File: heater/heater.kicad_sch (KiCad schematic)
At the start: 2 parts, among them J1 Conn_01x01, J2 Conn_01x01

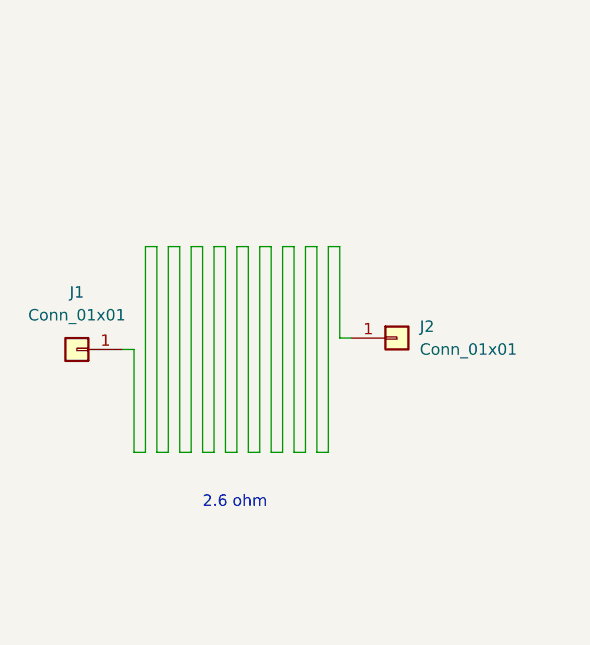
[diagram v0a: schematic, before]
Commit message: Design heating plate
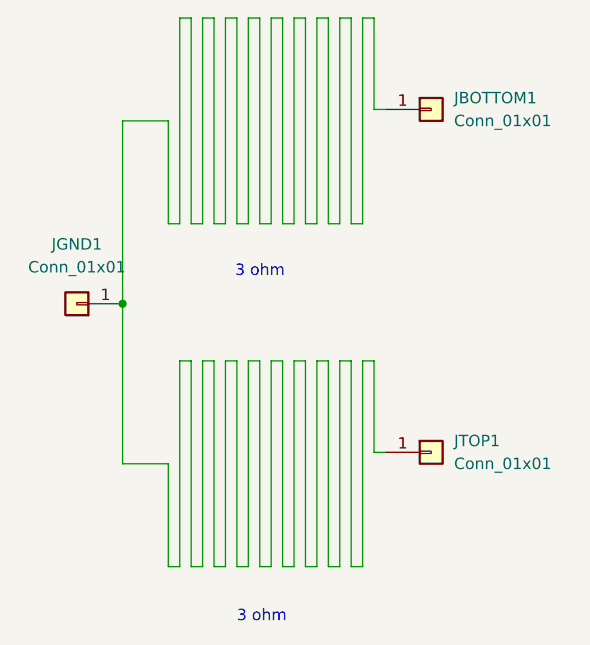
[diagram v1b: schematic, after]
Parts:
- added JTOP1: Conn_01x01, Library:MountingHole_3.2mm_Large, symbol Connector_Generic:Conn_01x01
- JBOTTOM1: renamed from J2; footprint (none) -> Library:MountingHole_3.2mm_Large
- JGND1: renamed from J1; footprint (none) -> Library:MountingHole_3.2mm_Large
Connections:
- net at JBOTTOM1.1 (Pin_1), JGND1.1 (Pin_1): now also JTOP1.1 (Pin_1)
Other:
- note added: "3 ohm"
- note removed: "2.6 ohm"
- moved on the sheet: JBOTTOM1, JGND1
